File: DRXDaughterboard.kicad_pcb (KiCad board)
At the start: 8 copper layers, 150.9 x 55.8 mm, 14 parts, among them J1 Samtec_ASP-134488-01, J2 Samtec_ASP-134488-01, J3 Conn_02x12_Odd_Even, J4 Samtec_ASP-134488-01, J5 Samtec_ASP-134488-01, J6 Conn_02x06_Odd_Even, J7 Samtec_ASP-134486-01, J8 Samtec_ASP-134486-01, U1 SN74LVC2T45DCUR

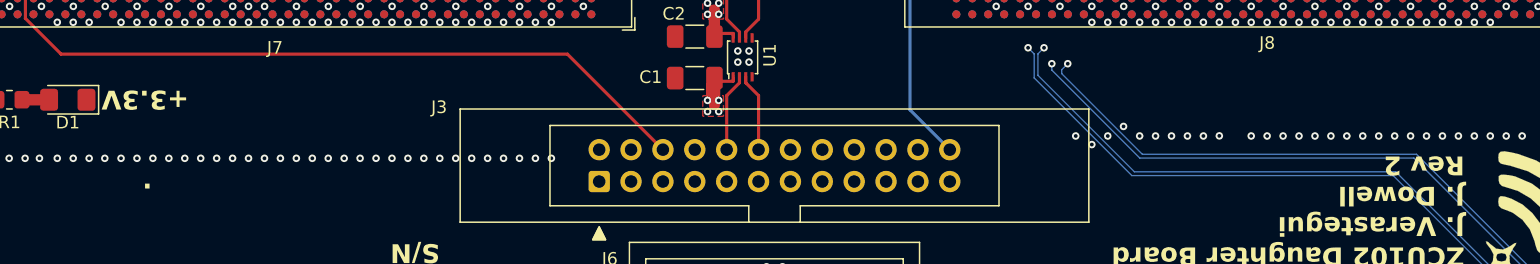
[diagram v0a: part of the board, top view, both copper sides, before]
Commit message: Fix ordering in the layer stackup.  Update the version.  Clean up some of the silkscreen.
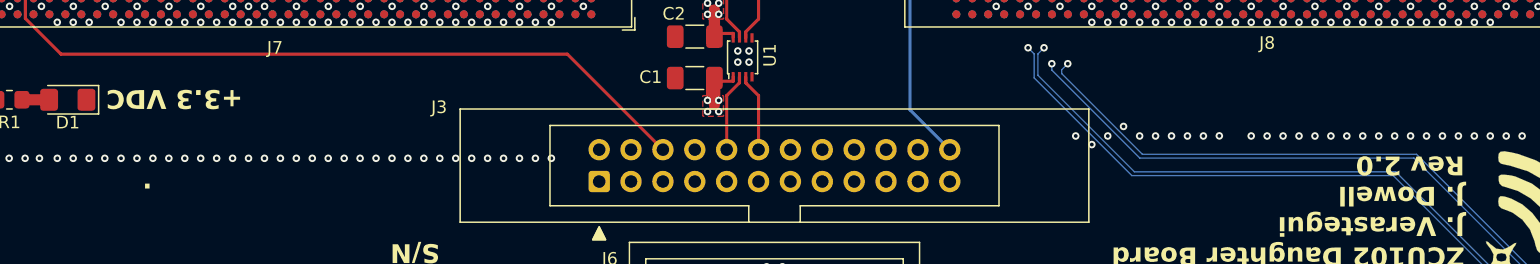
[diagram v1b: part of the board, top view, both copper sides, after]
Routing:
- added copper zone on In3.Cu, net +3.3VP
- removed copper zone on In4.Cu, net +3.3VP
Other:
- board text added: "+3.3 VDC"
- board text added: "ZCU102 Daughter Board J. Verastegui J. Dowell Rev 2.0"
- board text removed: "+3.3V"
- board text removed: "ZCU102 Daughter Board J. Verastegui J. Dowell Rev 2"
